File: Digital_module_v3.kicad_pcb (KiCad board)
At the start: 4 copper layers, 58.3 x 67.8 mm, 202 parts, among them J1 B2B-EH-A, J10 JoystickSwitch, J11 JoystickSwitch, J2 AUB-33, J3 AUB-33, J4 B2B-EH-A, J5 USB_B_Micro, J6 AUB-33, J7 AUB-33, J8 AUB-33, J9 SWD(PLS5), Q1 BSS138, Q10 BSS138, Q11 BSS138, Q12 BSS138, Q13 BSS138, Q14 BSS138, Q15 BSS138, Q16 2N5551S, Q17 BSS138, Q18 BSS138, Q19 BSS138, Q2 BSS138, Q20 BSS138, Q21 UMH3N, Q22 2N5551S, Q3 BSS138, Q4 BSS138, Q5 BSS138, Q6 BSS138, Q7 BSS138, Q8 BSS138, Q9 BSS138, SW1 SW_Rst, SW2 SW_RST, SW3 SW_FLASH, U1 Power_manager_2_v3_wo3D, U10 STM32G030K6Tx, U11 SN74LVC1G08DBVR, U12 CH340C, U13 ESP-12F, U14 FM24C64B, U15 AT24CS64-XHM, U16 AT24CS64-SSHM, U2 Fan_control_module_2_v3, U3 PCA9544APW, U4 PCF8563TS, U5 PCF8563TS, U6 LM1117-3.3, U7 USBLC6-2SC6, U8 SSD1306, U9 AP3216C, Y1 SC-32S 32.768KHz, Y2 CSTCE8M

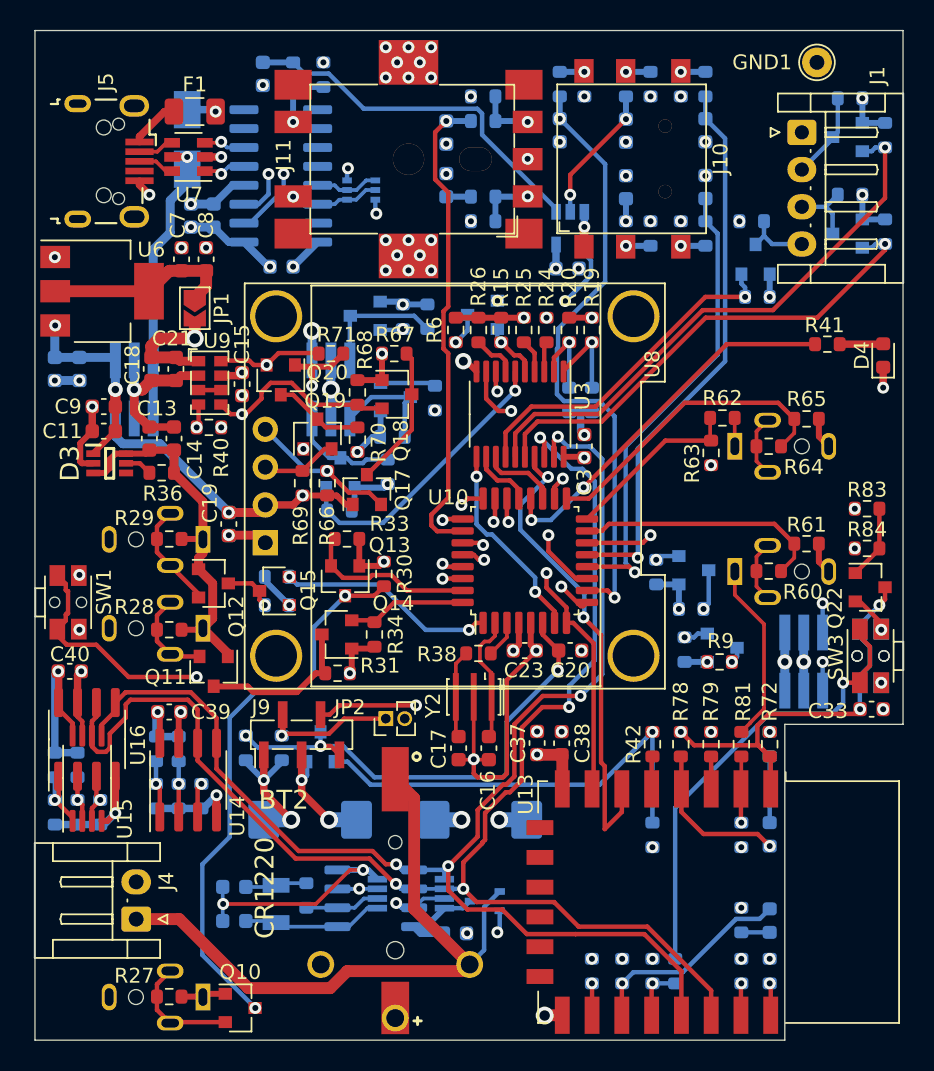
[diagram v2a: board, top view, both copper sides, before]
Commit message: Сформирован перечень элементов, 3D-модель, исправлены ошибки, реализована панелизация платы.
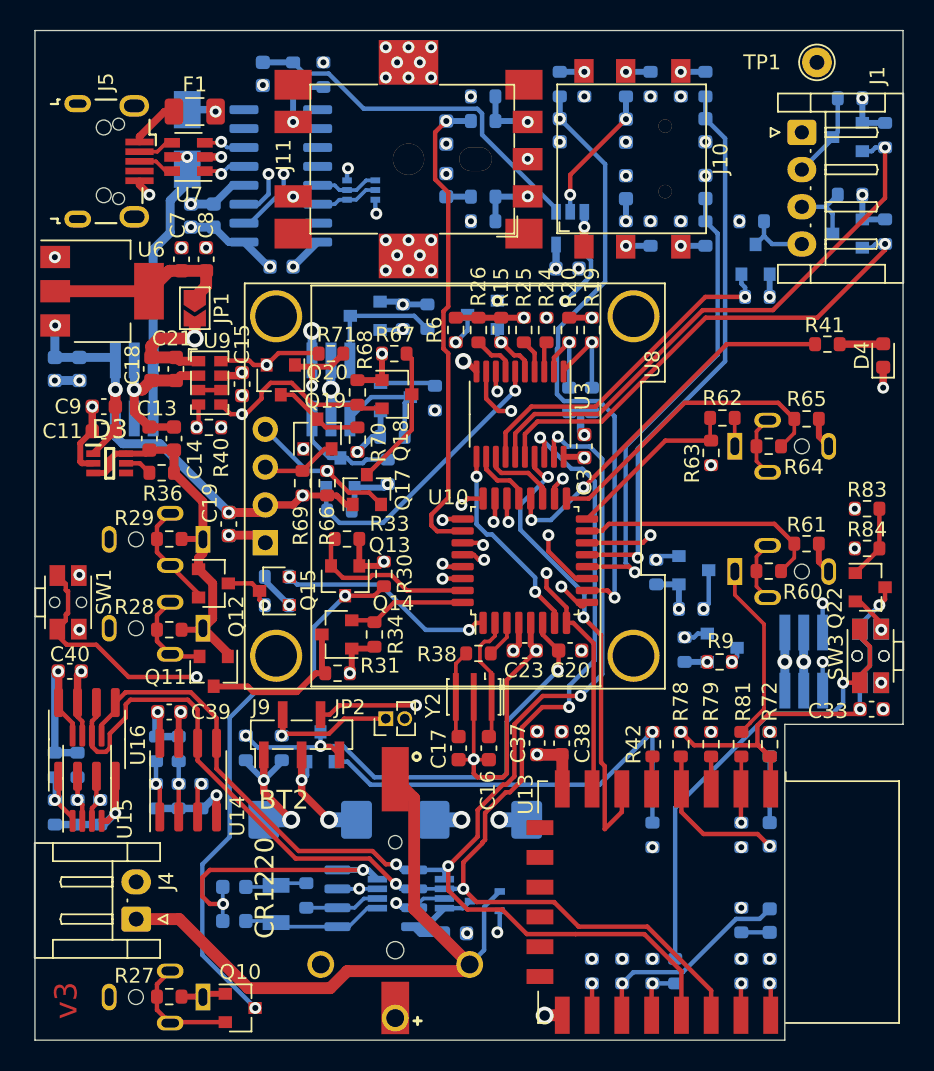
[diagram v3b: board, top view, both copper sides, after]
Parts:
- renumbered GND1 to TP1
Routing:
- net GND1: track 122.4 -> 126.0 mm
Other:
- board text added: "v3"

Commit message: Добавлен окантовка по контуру платы с двух сторон и текст: "JLCJLCJLCJLC"
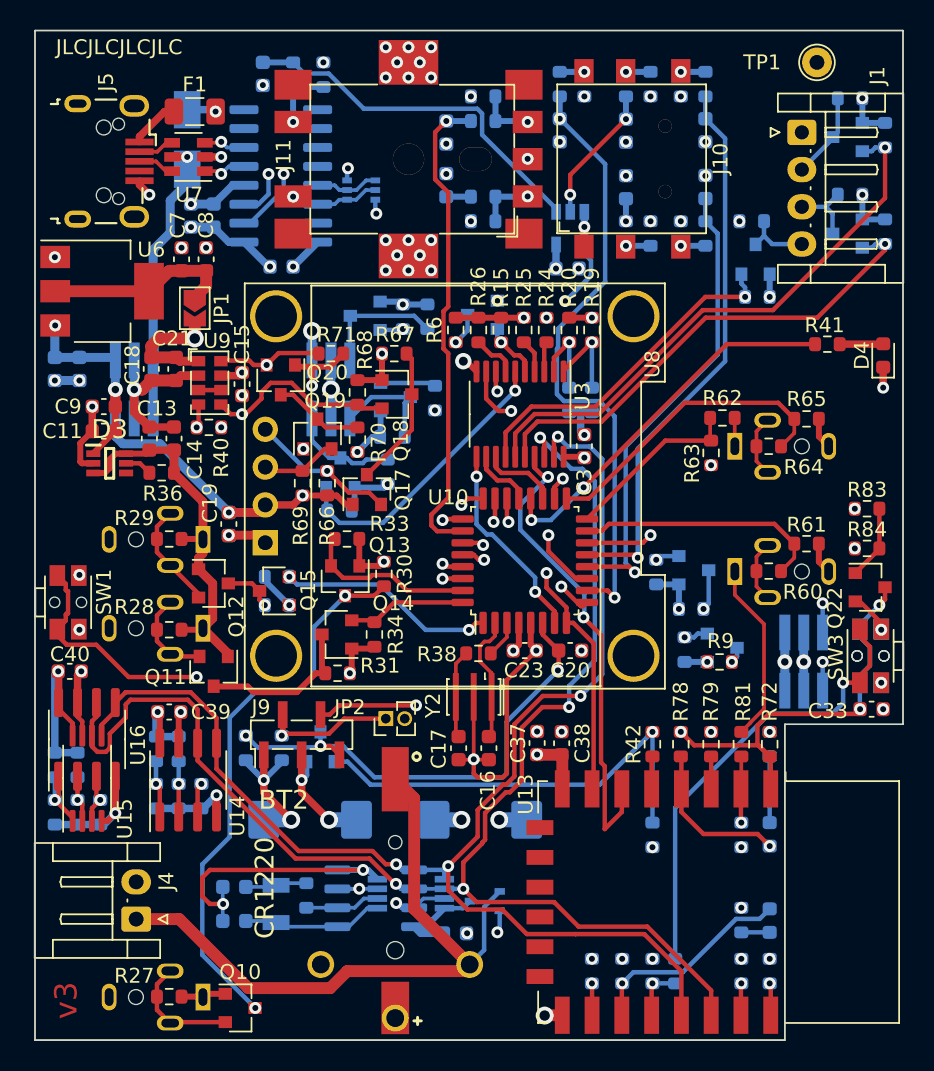
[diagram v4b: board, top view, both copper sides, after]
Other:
- board text added: "JLCJLCJLCJLC"

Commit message: Последние изменения в BOM
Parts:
- J1: value B2B-EH-A -> B4B-EH-A
